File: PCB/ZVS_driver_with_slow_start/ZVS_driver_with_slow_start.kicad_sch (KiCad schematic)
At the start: 31 parts, among them J1 Battery_12v_Connection, J2 Power_Switch, J3 ON_switch, J4 Conn_01x02_Socket, Q1 IRF640NPbF, Q2 IRF640NPbF, Q3 IRF640NPbF, U1 OP07, U2 OP07

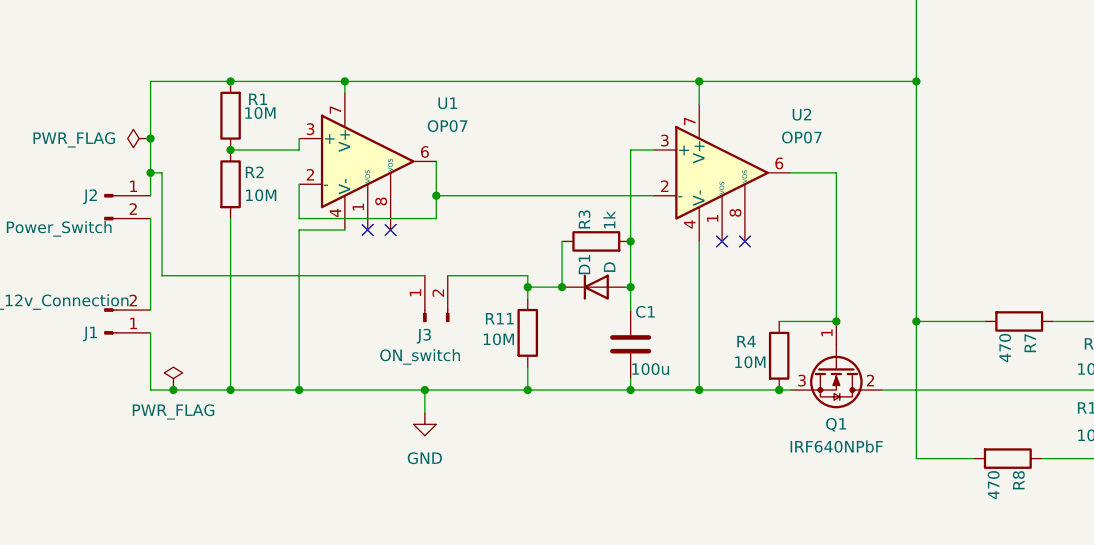
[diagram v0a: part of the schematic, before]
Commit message: added curent limiting RL on Q1
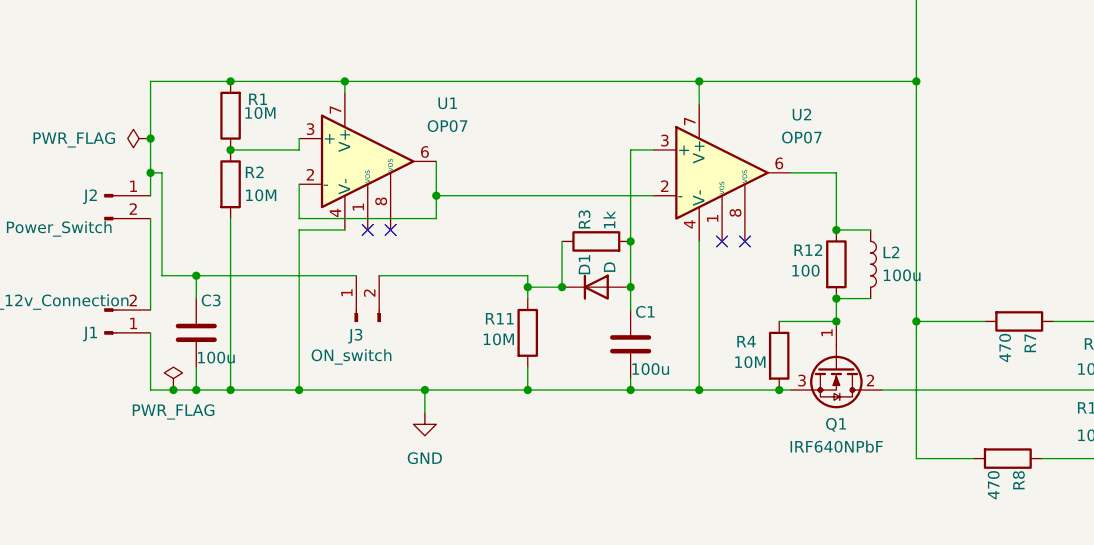
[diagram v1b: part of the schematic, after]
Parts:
- added C3: 100u, Capacitor_SMD:C_0805_2012Metric, symbol Device:C
- added L2: 100u, Inductor_SMD:L_Coilcraft_LPS4414, symbol Device:L
- added R12: 100, Resistor_SMD:R_0805_2012Metric, symbol Device:R
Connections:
- net GND: now also C3.2
- net at D3.1 (K), D4.1 (K), J2.1 (Pin_1)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: now also C3.1
- net at Q1.1 (G), R4.1: now also L2.2, R12.2; no longer U2.6
- new net: L2.1, R12.1, U2.6
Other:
- moved on the sheet: J3

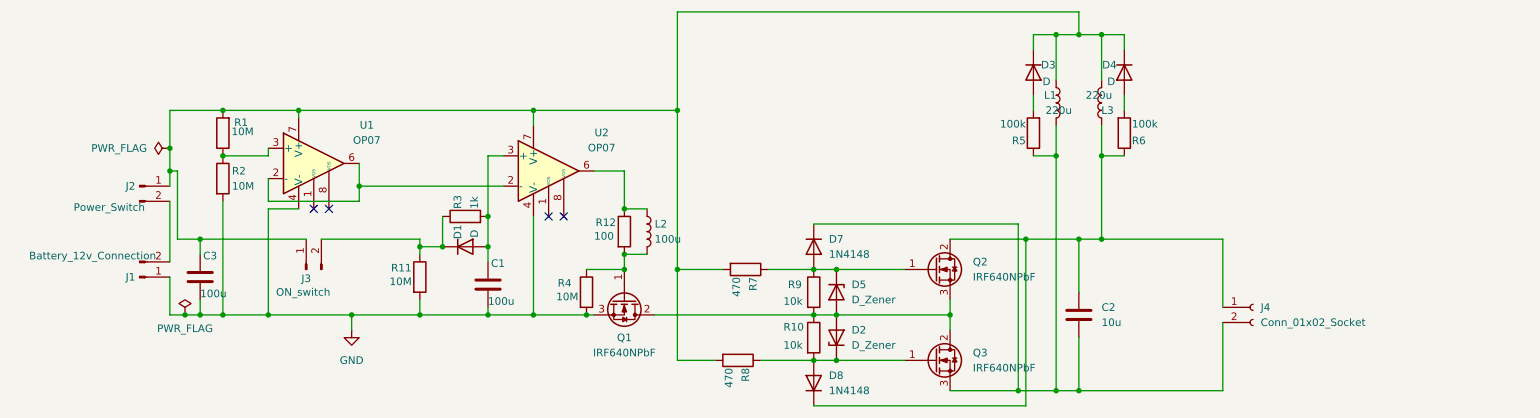
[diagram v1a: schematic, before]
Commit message: added fuse and cleaned up board
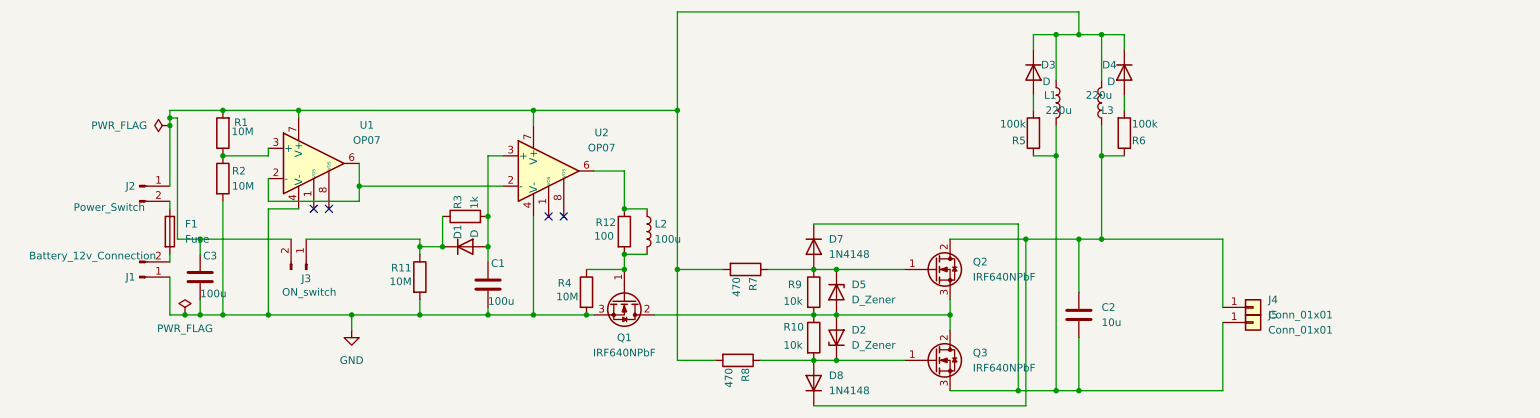
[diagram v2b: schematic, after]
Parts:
- removed J4: Conn_01x02_Socket, Connector_Wire:SolderWire-0.1sqmm_1x02_P3.6mm_D0.4mm_OD1mm, symbol Connector:Conn_01x02_Socket
- added F1: Fuse, Fuse:Fuseholder_Clip-5x20mm_Keystone_3517_Inline_P23.11x6.76mm_D1.70mm_Horizontal, symbol Device:Fuse
- added J4, J5: Conn_01x01, TerminalBlock_MetzConnect:TerminalBlock_MetzConnect_360271_1x01_Horizontal_ScrewM3.0_Boxed, symbol Connector_Generic:Conn_01x01
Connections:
- net at D1.1 (K), R11.1, R3.1: now also J3.1 (Pin_1); no longer J3.2 (Pin_2)
- net at C2.1, D8.1 (K), L3.1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: now also J4.1 (Pin_1)
- net at C3.1, D3.1 (K), D4.1 (K)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: now also J3.2 (Pin_2); no longer J3.1 (Pin_1)
- net at C2.2, D7.1 (K), L1.2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: now also J5.1 (Pin_1)
- net at J2.2 (Pin_2): now also F1.1; no longer J1.2 (Pin_2)
- new net: F1.2, J1.2 (Pin_2)
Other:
- moved on the sheet: J3

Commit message: the PCB is taking some serious shape
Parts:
- removed Q2: IRF640NPbF, Package_TO_SOT_THT:TO-220-3_Vertical, symbol NMOS_ME:Q_NMOS_DSG
- added Q4: IRF640NPbF, Package_TO_SOT_THT:TO-220-3_Vertical, symbol NMOS_ME:Q_NMOS_DSG
- added R13: 100M, Resistor_THT:R_Axial_DIN0411_L9.9mm_D3.6mm_P15.24mm_Horizontal, symbol Device:R
- C2: footprint Capacitor_THT:CP_Radial_D18.0mm_P7.50mm -> Capacitor_THT:C_Rect_L16.5mm_W9.0mm_P15.00mm_MKT
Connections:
- net GND: now also D2.2 (A), D5.2 (A), Q1.2 (D), Q3.3 (S), R10.1, R9.2, Q4.3 (S), R13.2
- net at C2.1, D8.1 (K), J4.1 (Pin_1): now also L1.2, R5.1, Q4.2 (D); no longer L3.1, R6.1
- net VBUS: now reaches C3.1, D3.1 (K), D4.1 (K), J2.1 (Pin_1), J3.2 (Pin_2), L1.1, L3.2, R1.2, R7.2, R8.2, U1.7 (V+), U2.7 (V+)
- net VBUS: now also F1.1, F1.2, J1.2 (Pin_2), J2.2 (Pin_2), R13.1
- net at C2.2, D7.1 (K), J5.1 (Pin_1): now also L3.1, Q3.2 (D), R6.1; no longer L1.2, Q3.3 (S), R5.1
- net at D5.1 (K), D7.2 (A), R7.1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: now also Q4.1 (G)
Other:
- moved on the sheet: C2, D2, D3, D4, D5, D7, D8, J4, J5, L1, L3, R10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

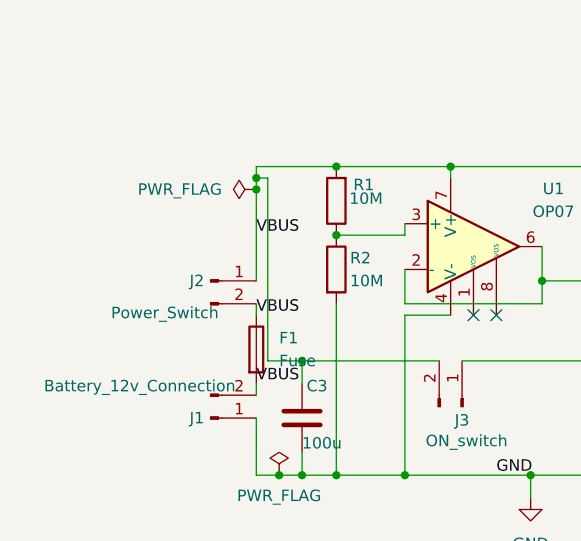
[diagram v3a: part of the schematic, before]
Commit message: removed superflous power switch
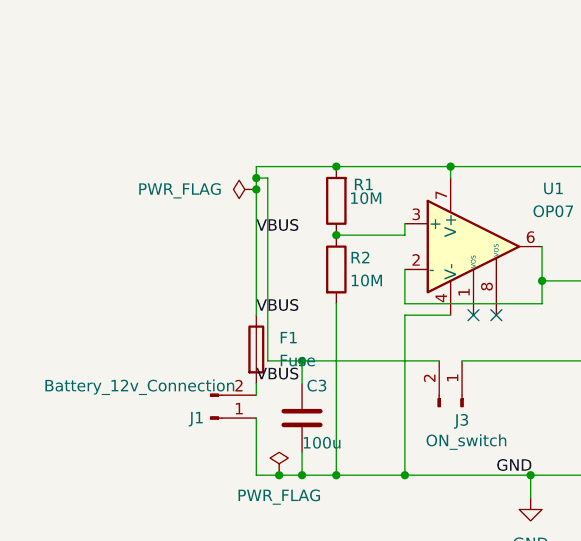
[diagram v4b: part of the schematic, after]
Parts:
- removed J2: Power_Switch, Connector_AMASS:AMASS_XT30U-F_1x02_P5.0mm_Vertical, symbol Connector:Conn_01x02_Pin
- R10, R7, R8, R9: footprint Resistor_SMD:R_0805_2012Metric -> Resistor_THT:R_Axial_DIN0207_L6.3mm_D2.5mm_P7.62mm_Horizontal
- R13, R5, R6: footprint Resistor_THT:R_Axial_DIN0411_L9.9mm_D3.6mm_P15.24mm_Horizontal -> Resistor_THT:R_Axial_DIN0207_L6.3mm_D2.5mm_P7.62mm_Horizontal
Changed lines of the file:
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@@
 	(wire
 		(pts
-			(xy 43.18 93.98) (xy 43.18 95.25)
-		)
-		(stroke
-			(width 0)
-			(type default)
-		)
-	)
-	(wire
-		(pts
 			(xy 158.75 62.23) (xy 226.06 62.23)
 		)
@@
 	(wire
 		(pts
-			(xy 43.18 81.28) (xy 43.18 91.44)
+			(xy 43.18 81.28) (xy 43.18 95.25)
 		)
 		(stroke
@@
 			)
 		)
-		(property "Footprint" "Resistor_THT:R_Axial_DIN0411_L9.9mm_D3.6mm_P15.24mm_Horizontal"
+		(property "Footprint" "Resistor_THT:R_Axial_DIN0207_L6.3mm_D2.5mm_P7.62mm_Horizontal"
 			(at 231.902 82.55 90)
 			(effects
@@
 			)
 		)
-		(property "Footprint" "Resistor_SMD:R_0805_2012Metric"
+		(property "Footprint" "Resistor_THT:R_Axial_DIN0207_L6.3mm_D2.5mm_P7.62mm_Horizontal"
 			(at 179.832 116.84 90)
 			(effects
@@
 			)
 		)
-		(property "Footprint" "Resistor_THT:R_Axial_DIN0411_L9.9mm_D3.6mm_P15.24mm_Horizontal"
+		(property "Footprint" "Resistor_THT:R_Axial_DIN0207_L6.3mm_D2.5mm_P7.62mm_Horizontal"
 			(at 220.218 82.55 90)
 			(effects
@@
 			)
 		)
-		(property "Footprint" "Resistor_SMD:R_0805_2012Metric"
+		(property "Footprint" "Resistor_THT:R_Axial_DIN0207_L6.3mm_D2.5mm_P7.62mm_Horizontal"
 			(at 170.18 103.632 90)
 			(effects
@@
 			)
 		)
-		(property "Footprint" "Resistor_SMD:R_0805_2012Metric"
+		(property "Footprint" "Resistor_THT:R_Axial_DIN0207_L6.3mm_D2.5mm_P7.62mm_Horizontal"
 			(at 179.832 109.22 90)
 			(effects
@@
 			)
 		)
-		(property "Footprint" "Resistor_THT:R_Axial_DIN0411_L9.9mm_D3.6mm_P15.24mm_Horizontal"
+		(property "Footprint" "Resistor_THT:R_Axial_DIN0207_L6.3mm_D2.5mm_P7.62mm_Horizontal"
 			(at 139.192 97.79 90)
 			(effects
@@
 			)
 		)
-		(property "Footprint" "Resistor_SMD:R_0805_2012Metric"
+		(property "Footprint" "Resistor_THT:R_Axial_DIN0207_L6.3mm_D2.5mm_P7.62mm_Horizontal"
 			(at 168.91 118.872 90)
 			(effects
@@
 					(unit 1)
 				)
-			)
-		)
-	)
-	(symbol
-		(lib_id "Connector:Conn_01x02_Pin")
-		(at 38.1 91.44 0)
-		(unit 1)
-		(exclude_from_sim no)
-		(in_bom yes)
-		(on_board yes)
-		(dnp no)
-		(property "Reference" "J2"
-			(at 36.576 91.44 0)
-			(effects
-				(font
-					(size 1.27 1.27)
-				)
-			)
-		)
-		(property "Value" "Power_Switch"
-			(at 33.02 94.996 0)
-			(effects
-				(font
-					(size 1.27 1.27)
-				)
-			)
-		)
-		(property "Footprint" "Connector_AMASS:AMASS_XT30U-F_1x02_P5.0mm_Vertical"
-			(at 38.1 91.44 0)
-			(effects
-				(font
-					(size 1.27 1.27)
-				)
-				(hide yes)
-			)
-		)
-		(property "Datasheet" "~"
-			(at 38.1 91.44 0)
-			(effects
-				(font
-					(size 1.27 1.27)
-				)
-				(hide yes)
-			)
-		)
-		(property "Description" "Generic connector, single row, 01x02, script generated"
-			(at 38.1 91.44 0)
-			(effects
-				(font
-					(size 1.27 1.27)
-				)
-				(hide yes)
-			)
-		)
-		(pin "1"
-		)
-		(pin "2"
-		)
-		(instances
-			(project "ZVS_driver_with_slow_start"
-				(path "/c49e841c-fad0-4812-b9c2-9ea62c8990ee"
-					(reference "J2")
-					(unit 1)
-				)
